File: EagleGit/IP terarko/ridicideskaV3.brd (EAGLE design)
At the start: 142.2 x 94.9 mm, 61 parts, among them IC1 74HC595N, IC2 74HC597N, Q3 32.768kHz

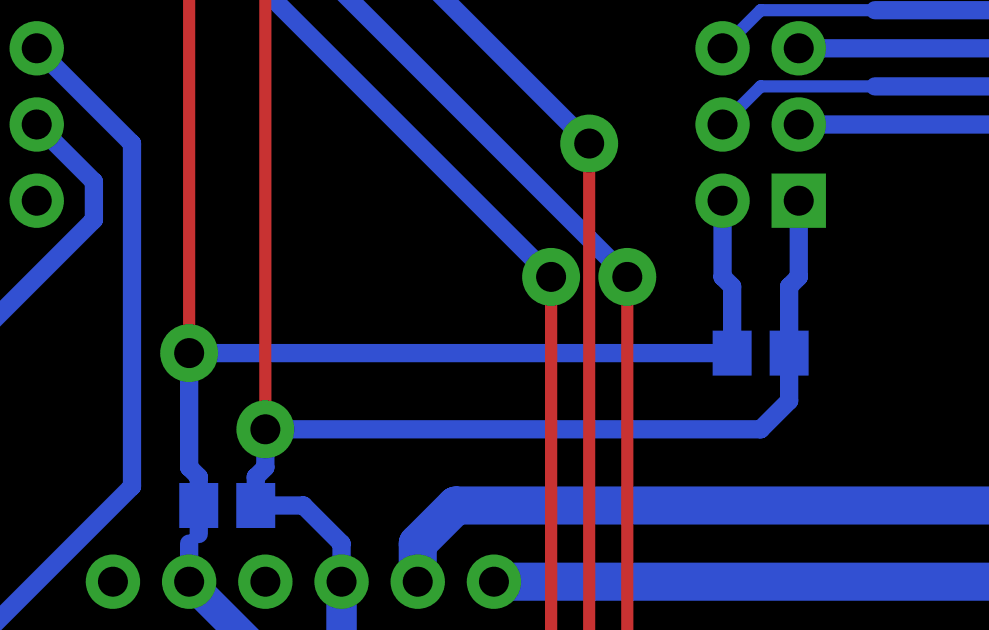
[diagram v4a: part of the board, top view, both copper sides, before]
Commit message: VDDA - odpojeno od napajeni, na desce discovery kitu je filtrovana hodnota
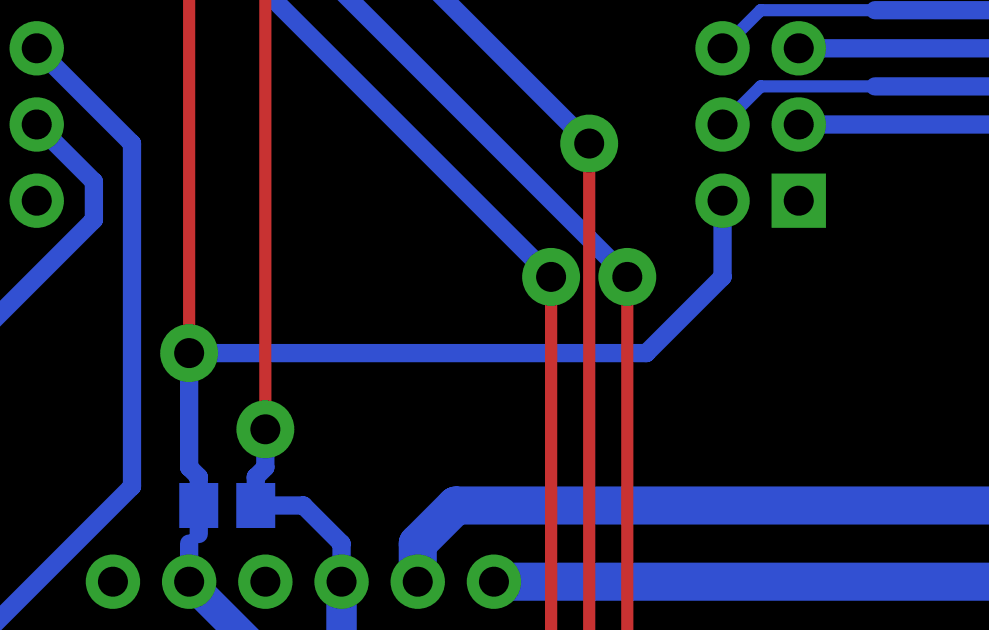
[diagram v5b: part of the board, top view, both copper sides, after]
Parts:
- removed C20: 10n, rcl:C0805
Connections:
- net GND: no longer C20.2
- net VDD_P: no longer C20.1, IO1.VDDA
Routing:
- net VDD_P: track 88.7 -> 64.0 mm
- net GND: track 282.9 -> 281.0 mm
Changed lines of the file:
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@@
 <element name="C18" library="rcl" package="C0805" value="10n" x="57.15" y="78.74" rot="MR0"/>
 <element name="C19" library="rcl" package="C0805" value="10n" x="57.15" y="49.53" rot="MR0"/>
-<element name="C20" library="rcl" package="C0805" value="10n" x="74.93" y="54.61" rot="MR0"/>
 <element name="R18" library="rcl" package="0207/12" value="1k" x="32.7025" y="19.685" rot="R90"/>
 <element name="R19" library="rcl" package="0207/12" value="1k" x="30.48" y="40.64"/>
@@
 <wire x1="56.2" y1="78.74" x2="56.2" y2="80.33" width="0.4064" layer="16"/>
 <wire x1="56.2" y1="80.33" x2="57.15" y2="81.28" width="0.4064" layer="16"/>
-<contactref element="C20" pad="2"/>
-<wire x1="55.88" y1="54.61" x2="73.98" y2="54.61" width="0.6096" layer="16"/>
-<wire x1="73.66" y1="59.69" x2="73.66" y2="57.15" width="0.6096" layer="16"/>
-<wire x1="73.98" y1="54.61" x2="73.98" y2="56.83" width="0.6096" layer="16"/>
-<wire x1="73.98" y1="56.83" x2="73.66" y2="57.15" width="0.6096" layer="16"/>
 <wire x1="139.7" y1="55.88" x2="139.7" y2="66.04" width="1.27" layer="16"/>
 <wire x1="139.7" y1="10.16" x2="139.7" y2="7.62" width="1.27" layer="16"/>
@@
 <wire x1="138.43" y1="86.36" x2="139.7" y2="85.09" width="1.27" layer="16"/>
 <wire x1="139.7" y1="85.09" x2="139.7" y2="83.82" width="1.27" layer="16"/>
+<wire x1="55.88" y1="54.61" x2="71.12" y2="54.61" width="0.6096" layer="16"/>
+<wire x1="71.12" y1="54.61" x2="73.66" y2="57.15" width="0.6096" layer="16"/>
+<wire x1="73.66" y1="57.15" x2="73.66" y2="59.69" width="0.6096" layer="16"/>
 </signal>
 <signal name="VDD">
@@
 <contactref element="IO1" pad="VDD"/>
 <contactref element="IO1" pad="VDDIO_2"/>
-<contactref element="IO1" pad="VDDA"/>
 <contactref element="C9" pad="1"/>
 <wire x1="60.96" y1="44.45" x2="60.96" y2="46.99" width="1.016" layer="16"/>
@@
 <wire x1="58.1" y1="79.69" x2="58.42" y2="80.01" width="0.4064" layer="16"/>
 <wire x1="58.42" y1="80.01" x2="58.42" y2="82.55" width="0.4064" layer="16"/>
-<contactref element="C20" pad="1"/>
-<wire x1="75.88" y1="53.02" x2="74.93" y2="52.07" width="0.6096" layer="16"/>
-<wire x1="74.93" y1="52.07" x2="58.42" y2="52.07" width="0.6096" layer="16"/>
-<wire x1="75.88" y1="54.61" x2="75.88" y2="53.02" width="0.6096" layer="16"/>
-<wire x1="76.2" y1="59.69" x2="76.2" y2="57.15" width="0.6096" layer="16"/>
-<wire x1="75.88" y1="54.61" x2="75.88" y2="56.83" width="0.6096" layer="16"/>
-<wire x1="75.88" y1="56.83" x2="76.2" y2="57.15" width="0.6096" layer="16"/>
 <wire x1="62.23" y1="38.1" x2="62.23" y2="40.64" width="1.016" layer="16"/>
 <wire x1="62.23" y1="40.64" x2="60.96" y2="41.91" width="1.016" layer="16"/>

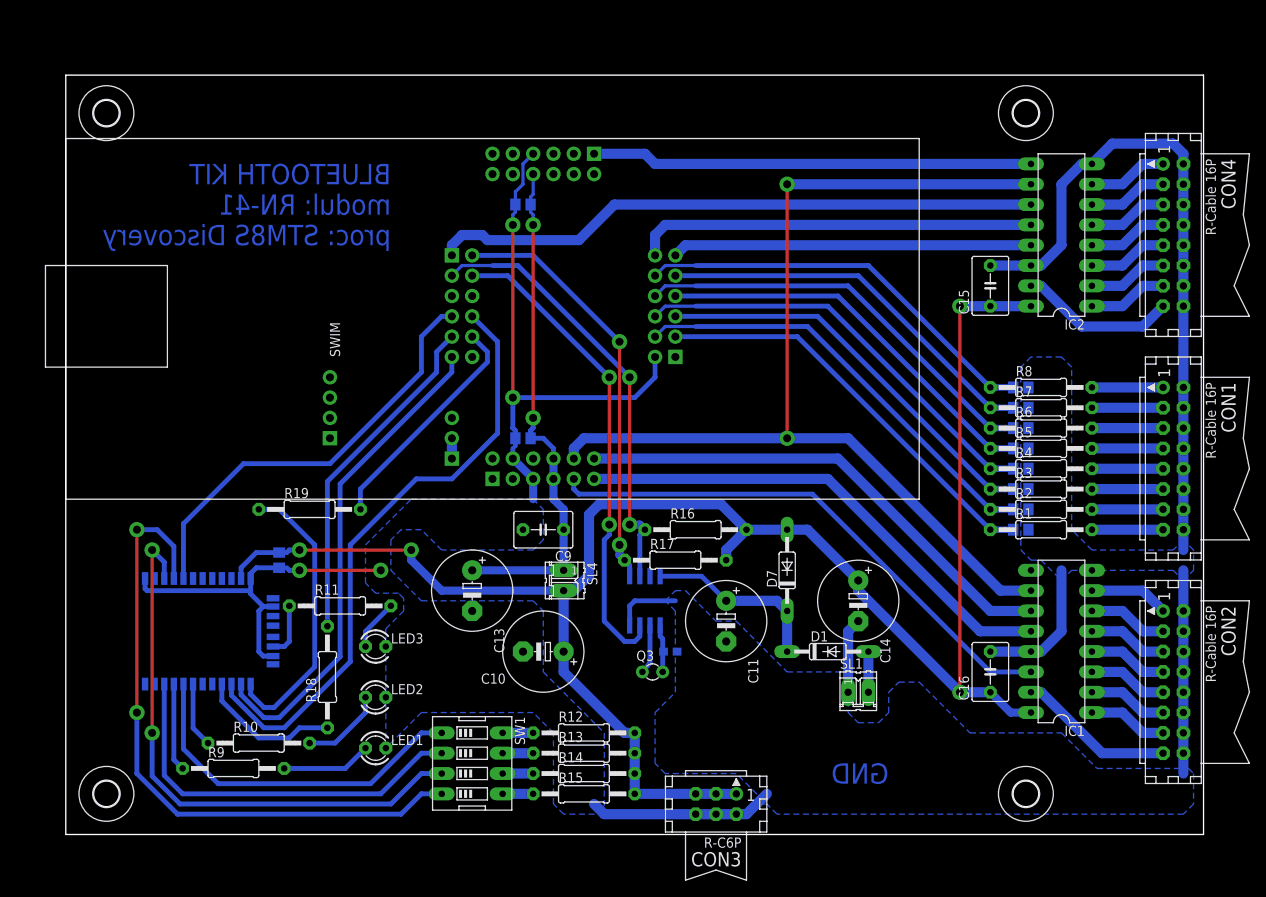
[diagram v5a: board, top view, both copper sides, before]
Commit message: Terarko: -na DPS pridan napajeci konektor -na DPS pridan konektor SPI -opraveny vsechny cesty
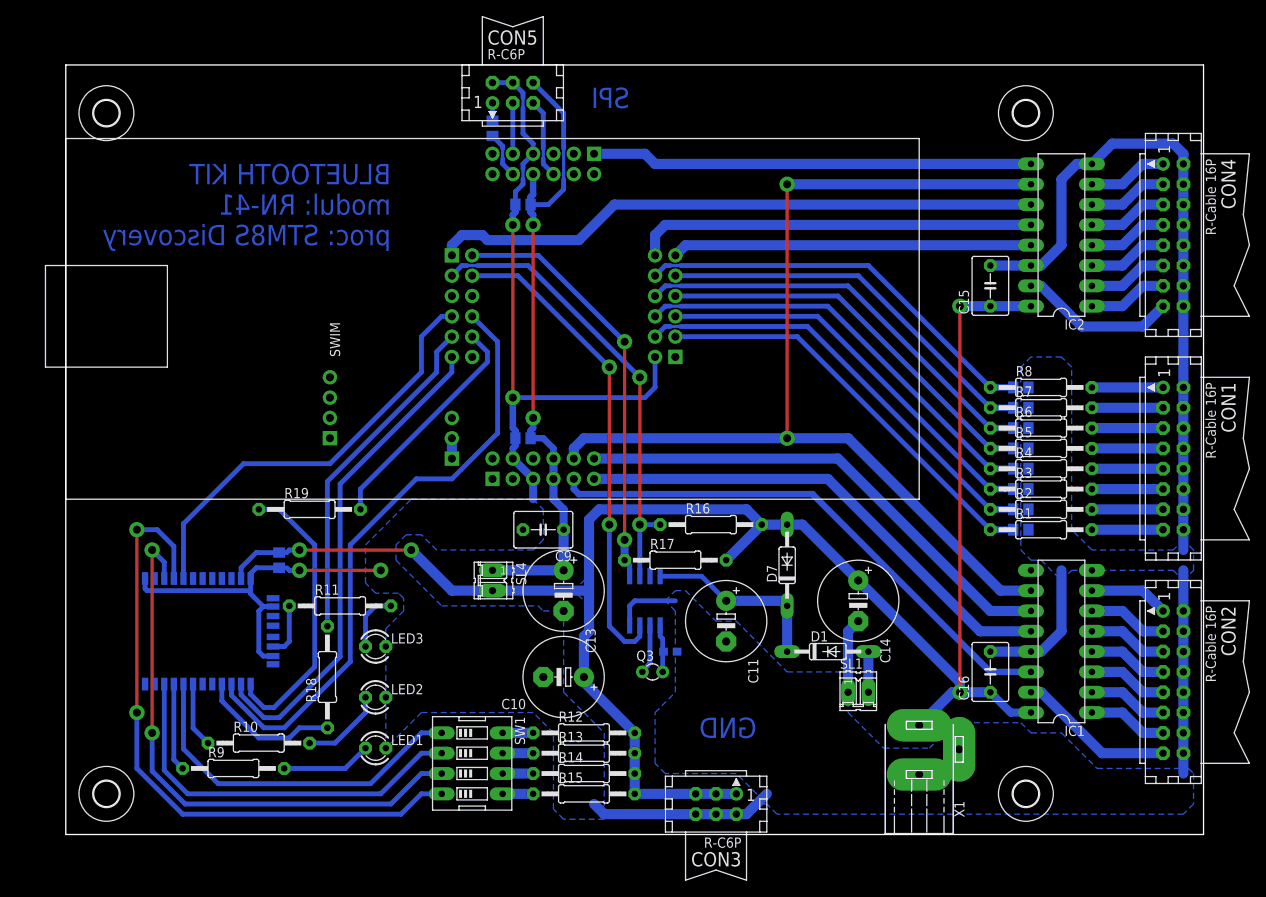
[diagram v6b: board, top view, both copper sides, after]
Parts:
- added CON5: (no value), con-harting:CON06
- added R20: 150R, rcl:R0805
- added X1: (no value), con-conrad:733980-62
- moved C13 11.4 mm to (62.2, 30.5)
- moved SL4 8.89 mm to (53.3, 31.8)
- moved C10 4.07 mm to (62.2, 19.7)
- moved R16 2.01 mm to (80.6, 38.7)
- moved D7 0.63 mm to (90.2, 33.7)
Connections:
- new net N$70: IO1.PC7, R20.1
- new net N$71: CON5.1, R20.2
- new net N$72: CON5.3, IO1.PC6
- new net N$73: CON5.5, IO1.PC5
- net GND: now also CON5.2, CON5.4, X1.2, X1.3
- net VDD: now also X1.1
- net VDD_P: now also CON5.6
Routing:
- net VDD_P: track 64.0 -> 81.3 mm
- net GND: track 281.0 -> 294.6 mm
- net N$73: track 0.00 -> 9.94 mm
- net N$72: track 0.00 -> 6.35 mm
- net VDD: track 228.8 -> 235.0 mm
- net N$70: track 0.00 -> 5.82 mm
- net N$71: track 0.00 -> 2.22 mm
- net N$28: track 55.2 -> 57.2 mm
- net N$58: track 6.40 -> 7.51 mm
- added copper zone on layer 16, net VDD
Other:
- board size 142.2 x 94.9 mm -> 142.2 x 96.2 mm
- board text added: "SPI"
